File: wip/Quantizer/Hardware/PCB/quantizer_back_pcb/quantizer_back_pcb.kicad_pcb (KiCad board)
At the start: 2 copper layers, 40 x 100 mm, 42 parts, among them J1 Conn_02x08_Odd_Even, J13 Conn_01x12_Male, J14 Conn_01x04_Male, J15 Conn_01x04_Male, J16 Conn_01x02_Male, Q1 2N3906, Q2 2N3906, U1 TL072, U2 TL074, U3 MCP4922, U4 TLC5940NT

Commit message: fixed Quantizer PCB
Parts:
- renumbered H2 to H1
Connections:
- A1 pad 19: Net-(A1-Pad19) -> BUTTON_LADDER
- A1 pad 5: Net-(A1-Pad5) -> MENU_BUTTON
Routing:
- net BUTTON_LADDER: track 0.00 -> 51.3 mm, vias 0 -> 1
- net MENU_BUTTON: track 0.00 -> 22.9 mm, vias 0 -> 1
- net GND: track 230.6 -> 233.7 mm
- net TRIG_B: track 57.5 -> 59.8 mm
- net TRIG_A: track 22.3 -> 23.7 mm
- removed copper zone on B.Cu, net GND
- removed copper zone on F.Cu, net GND

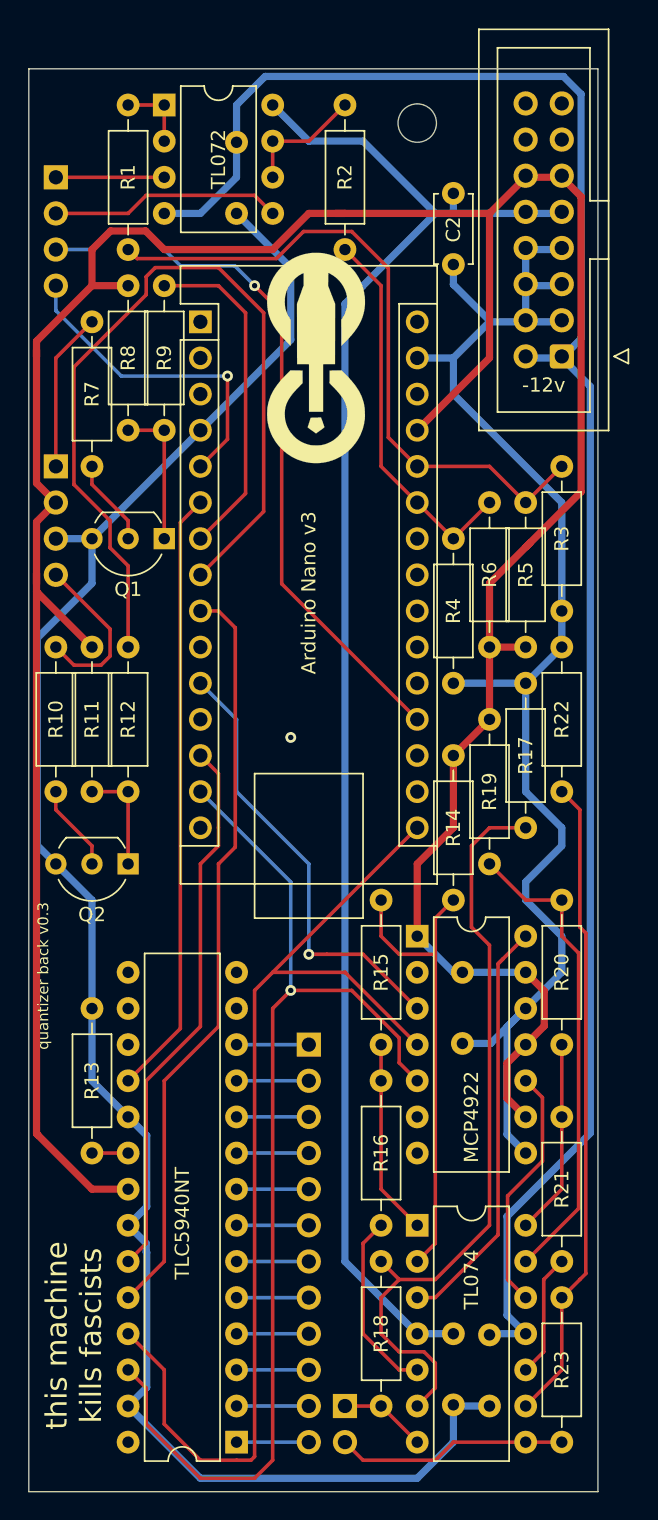
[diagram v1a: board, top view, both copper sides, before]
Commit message: fixed quantizer
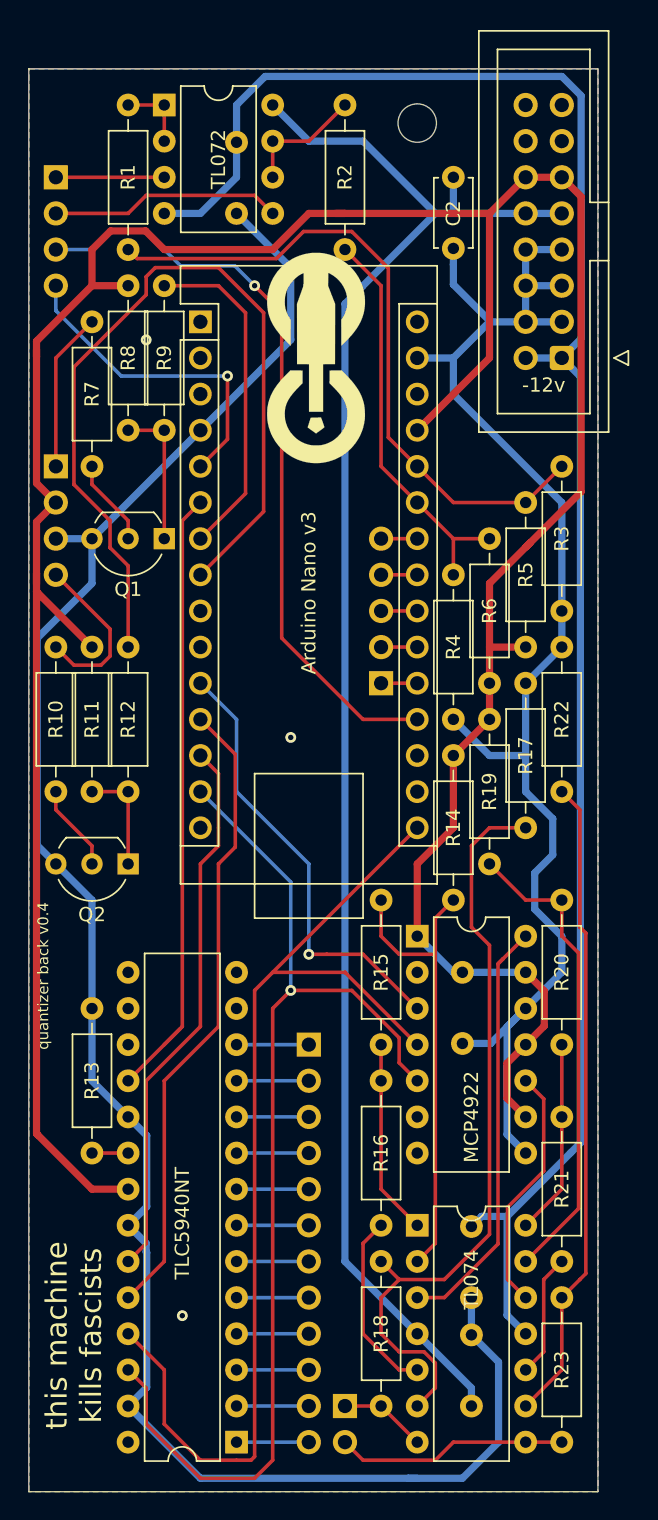
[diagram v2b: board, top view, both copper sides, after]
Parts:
- added J2: Conn_01x05_Female, Connector_PinHeader_2.54mm:PinHeader_1x05_P2.54mm_Vertical, B.Cu at (50.8, 63.5)
- moved C5 7.73 mm to (57.1, 106.7)
- moved C4 5.24 mm to (57.1, 114.3), turned to 90 degrees
- moved R4 2.54 mm to (55.9, 66.0)
- moved R6 2.54 mm to (58.4, 53.3)
- moved C2 1.13 mm to (55.9, 27.9)
- moved J1 0.11 mm to (63.5, 40.6)
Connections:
- A1 pad 12: Net-(A1-Pad12) -> TLC_XLAT
- A1 pad 9: TLC_XLAT -> Net-(A1-Pad9)
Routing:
- net GND: track 233.7 -> 244.4 mm, vias 1 -> 4
- net TLC_XLAT: track 53.1 -> 44.8 mm
- net +12V: track 110.9 -> 116.1 mm
- net Net-(A1-Pad24): track 0.00 -> 2.54 mm
- net Net-(A1-Pad23): track 0.00 -> 2.54 mm
- net Net-(A1-Pad22): track 0.00 -> 2.54 mm
- net Net-(A1-Pad21): track 0.00 -> 2.54 mm
- net Net-(A1-Pad20): track 0.00 -> 2.54 mm
- net BUTTON_LADDER: track 51.3 -> 53.5 mm
- net TLC_GSCLK: track 42.7 -> 44.3 mm
- net INPUT_B: track 27.1 -> 28.6 mm
- added copper zone on B.Cu, net GND
- added copper zone on F.Cu, net GND
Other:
- board text added: "quantizer back v0.4"
- board text removed: "quantizer back v0.3"
